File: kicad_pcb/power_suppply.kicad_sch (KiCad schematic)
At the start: 25 parts, among them J201 Barrel_Jack, J202 GND, J203 DC Power, J204 -8V, J205 +8V, U201 LM317L, U202 UA78M08, U203 UA79M08, U204 TLE2426xP

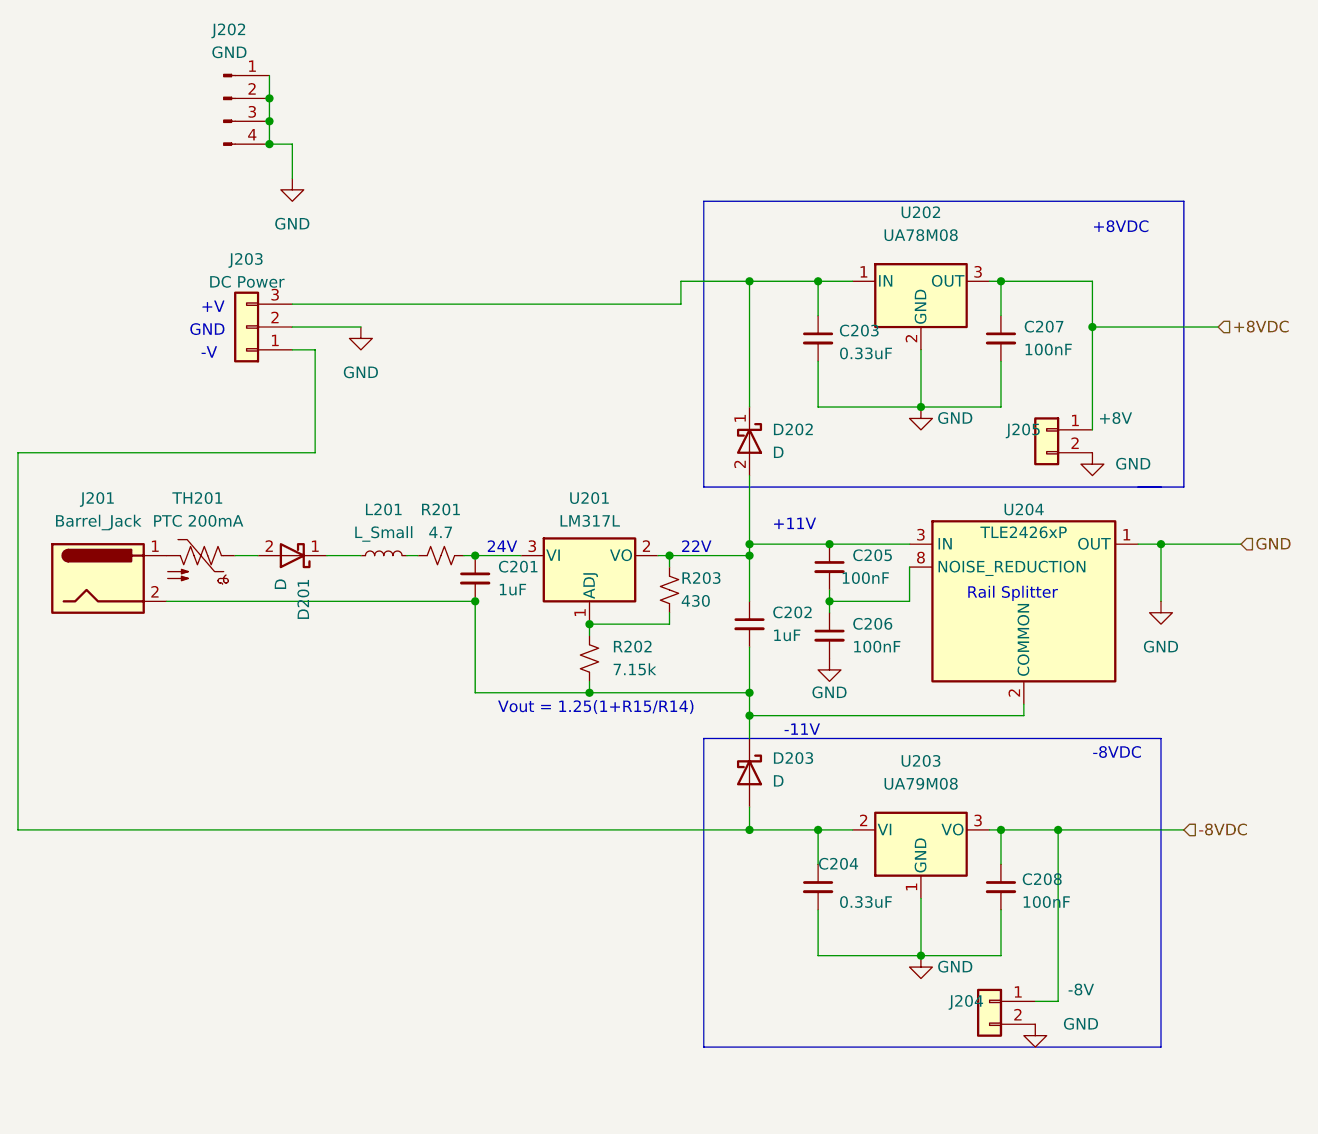
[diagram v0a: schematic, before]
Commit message: Update to KiCad 7. Added some freecad parts (unfortunately, thoroughly broken).
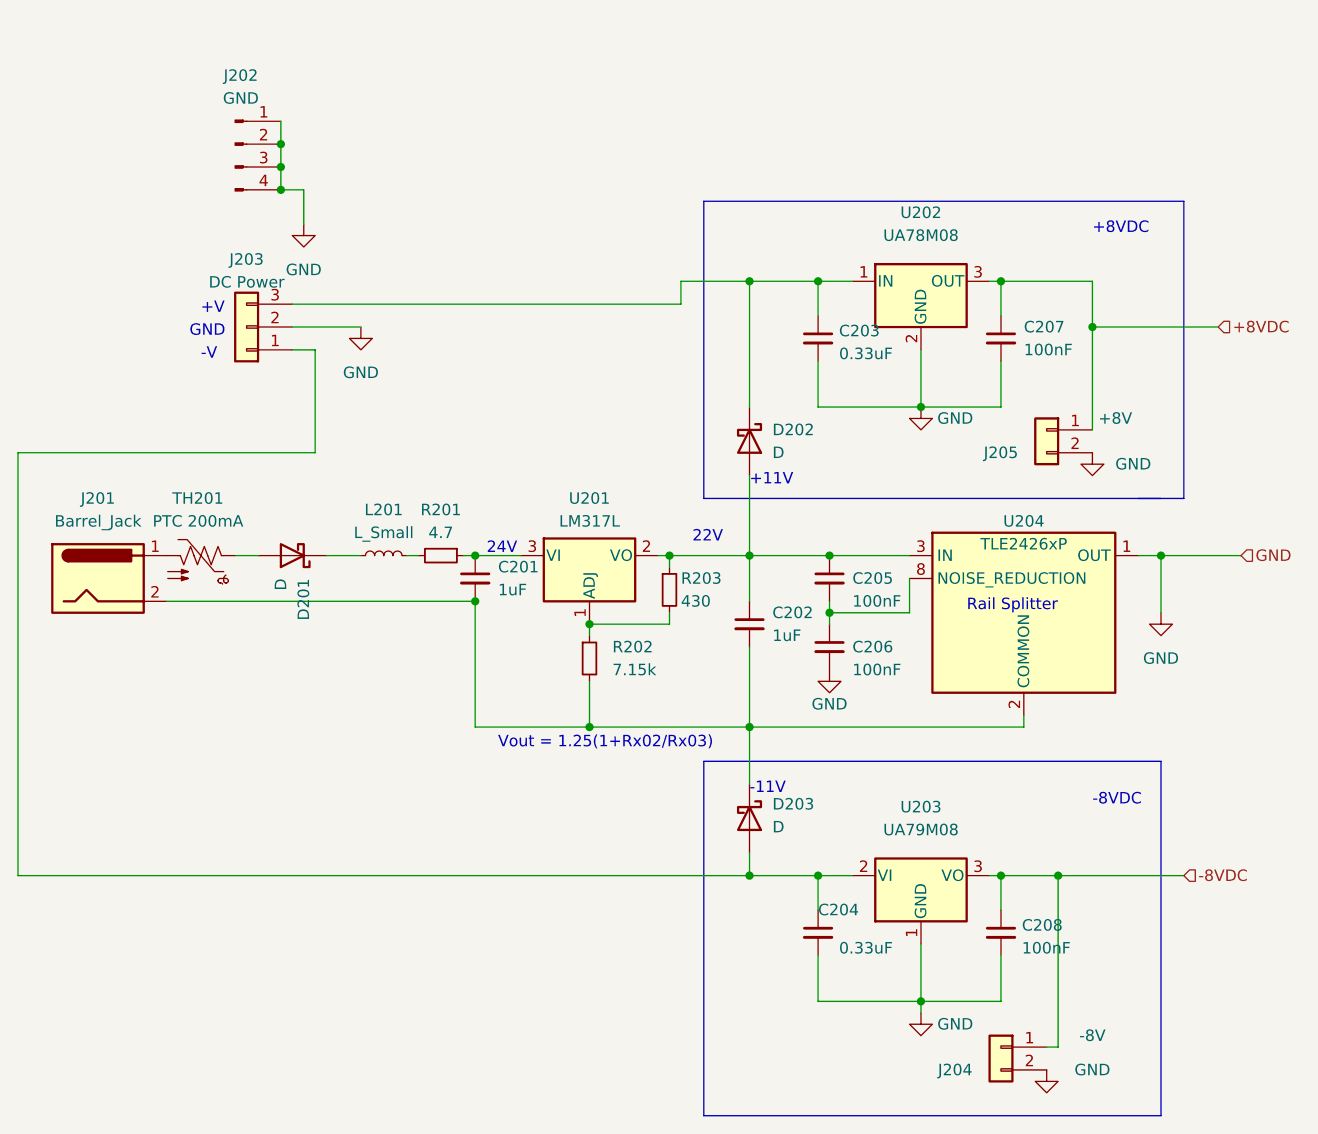
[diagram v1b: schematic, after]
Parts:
- J202: symbol Connector:Conn_01x04_Male -> Connector:Conn_01x04_Pin
- R201: symbol Device:R_Small_US -> Device:R_Small; Mouser 667-ERJ-P06F4300V -> 279-35224R7JT
- R202, R203: symbol Device:R_Small_US -> Device:R_Small
- U201: Mouser 595-LM317LCPK -> 595-LM317LIPKG3
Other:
- note added: "Vout = 1.25(1+Rx02/Rx03)"
- note removed: "Vout = 1.25(1+R15/R14)"
- moved on the sheet: C204, C205, C206, C208, D203, J202, J204, U203, U204
